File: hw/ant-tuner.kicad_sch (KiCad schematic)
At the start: 4 parts, among them K7702 G2RL-2, K7703 G2RL-2, K7704 G2RL-2

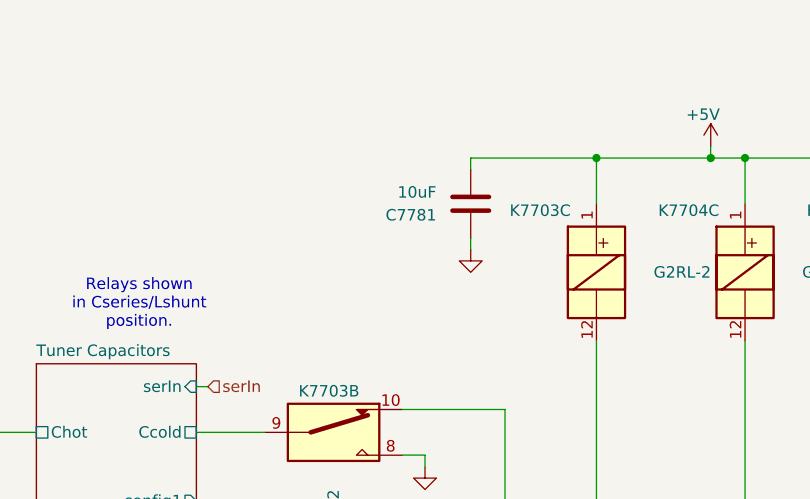
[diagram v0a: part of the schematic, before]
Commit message: Last rites for 800 ohm rx preselector, and probably the RF deck which was stillborn
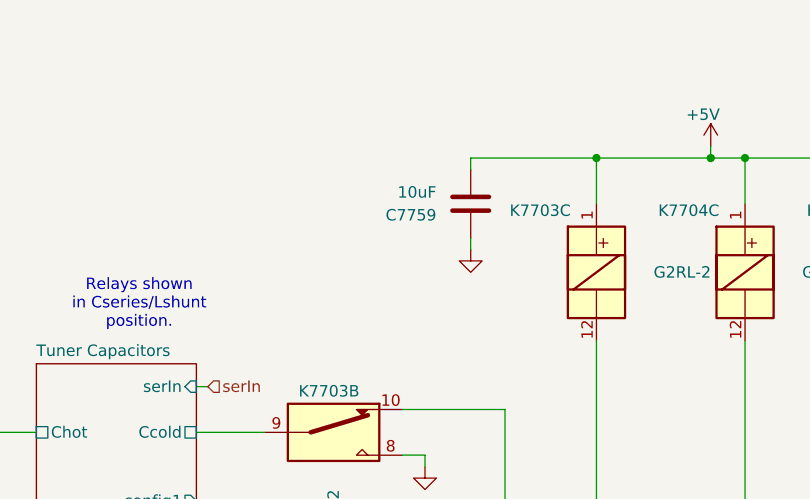
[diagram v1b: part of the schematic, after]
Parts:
- renumbered C7781 to C7759
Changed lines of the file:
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@@
 	(title_block
 		(title "Antenna Tuner")
-		(date "2025-10-30")
+		(date "2025-10-13")
 		(company "WB7NAB")
 		(comment 1 "Alan Mimms")
@@
 		(dnp no)
 		(fields_autoplaced yes)
-		(property "Reference" "#PWR07847"
+		(property "Reference" "#PWR07787"
 			(at 107.95 49.53 0)
 			(effects
@@
 			(project ""
 				(path "/8ae46c04-d01a-4756-8774-512b694bfaff/2406d03c-531b-4eaf-8b4b-4b266b9d0f2b/99bbdde6-e23e-4e3f-9a6c-8b2d863ddc64"
-					(reference "#PWR07847")
+					(reference "#PWR07787")
 					(unit 1)
 				)
@@
 		(dnp no)
 		(fields_autoplaced yes)
-		(property "Reference" "#PWR07846"
+		(property "Reference" "#PWR07786"
 			(at 105.41 106.68 0)
 			(effects
@@
 			(project "NexRig"
 				(path "/8ae46c04-d01a-4756-8774-512b694bfaff/2406d03c-531b-4eaf-8b4b-4b266b9d0f2b/99bbdde6-e23e-4e3f-9a6c-8b2d863ddc64"
-					(reference "#PWR07846")
+					(reference "#PWR07786")
 					(unit 1)
 				)
@@
 		(dnp no)
 		(fields_autoplaced yes)
-		(property "Reference" "#PWR07845"
+		(property "Reference" "#PWR07785"
 			(at 102.87 73.66 0)
 			(effects
@@
 			(project "NexRig"
 				(path "/8ae46c04-d01a-4756-8774-512b694bfaff/2406d03c-531b-4eaf-8b4b-4b266b9d0f2b/99bbdde6-e23e-4e3f-9a6c-8b2d863ddc64"
-					(reference "#PWR07845")
+					(reference "#PWR07785")
 					(unit 1)
 				)
@@
 		(on_board yes)
 		(dnp no)
-		(property "Reference" "C7781"
+		(property "Reference" "C7759"
 			(at 104.14 39.3701 0)
 			(effects
@@
 			(project "NexRig"
 				(path "/8ae46c04-d01a-4756-8774-512b694bfaff/2406d03c-531b-4eaf-8b4b-4b266b9d0f2b/99bbdde6-e23e-4e3f-9a6c-8b2d863ddc64"
-					(reference "C7781")
+					(reference "C7759")
 					(unit 1)
 				)
@@
 		(on_board yes)
 		(dnp no)
-		(property "Reference" "#PWR07848"
+		(property "Reference" "#PWR07788"
 			(at 134.62 35.56 0)
 			(effects
@@
 			(project "NexRig"
 				(path "/8ae46c04-d01a-4756-8774-512b694bfaff/2406d03c-531b-4eaf-8b4b-4b266b9d0f2b/99bbdde6-e23e-4e3f-9a6c-8b2d863ddc64"
-					(reference "#PWR07848")
+					(reference "#PWR07788")
 					(unit 1)
 				)

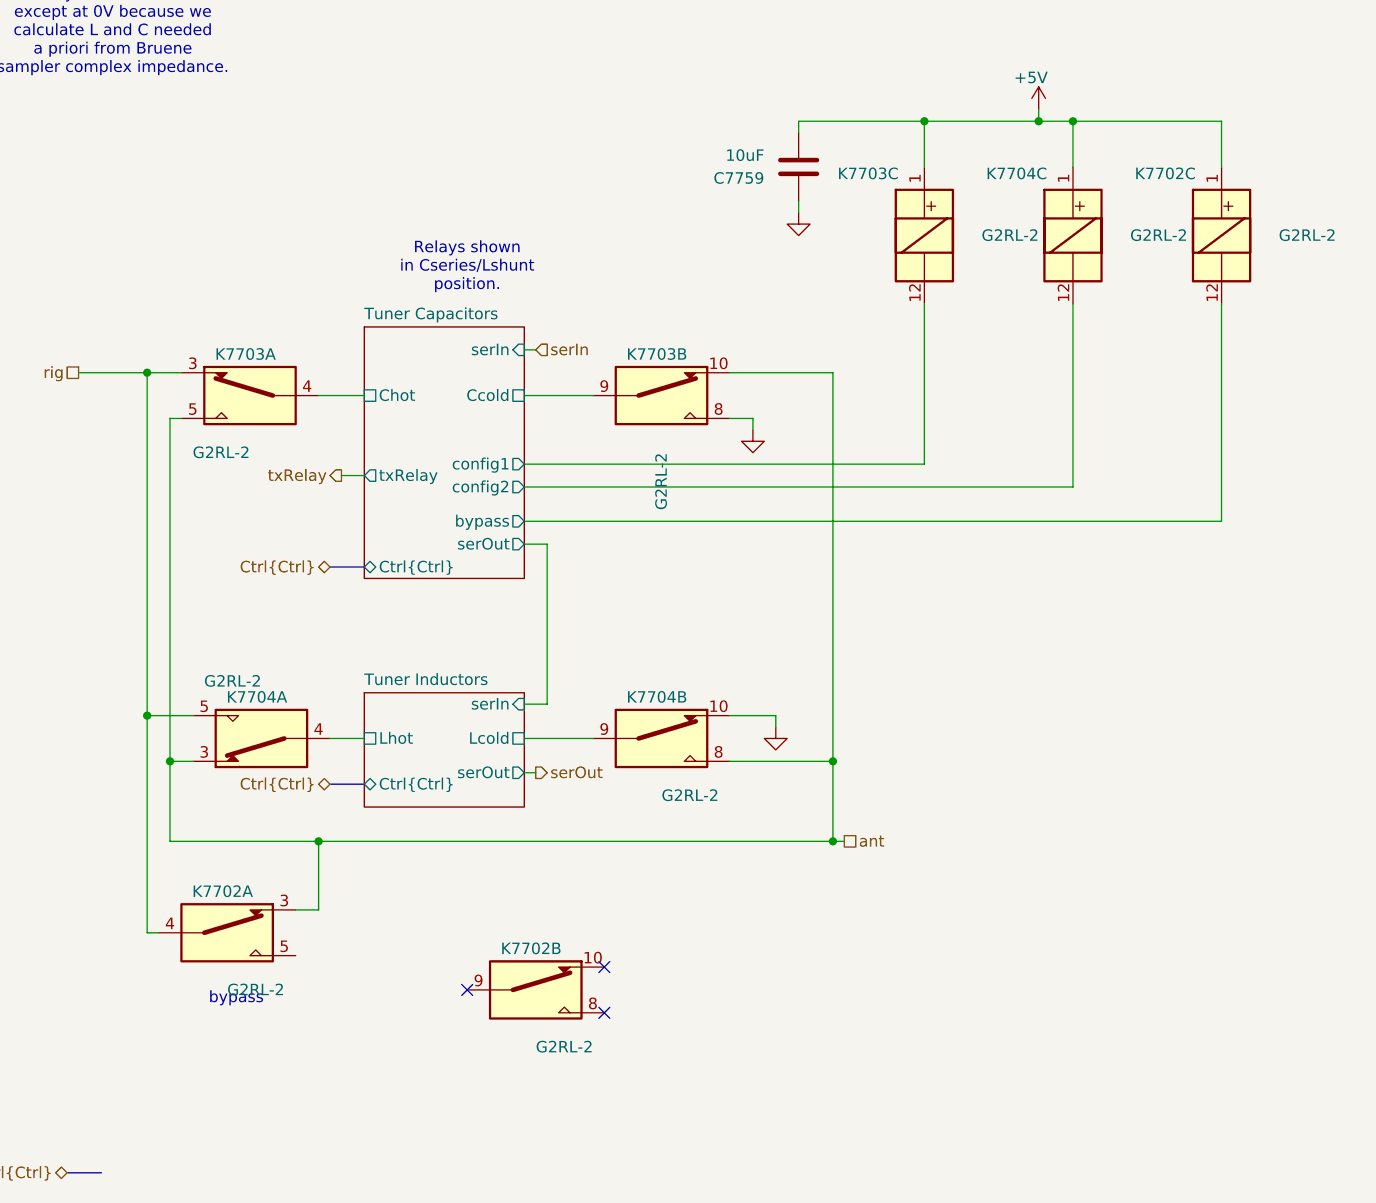
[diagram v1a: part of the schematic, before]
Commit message: Fixed GPIO assignments. Fixed symbol for GRL2-2 relays.
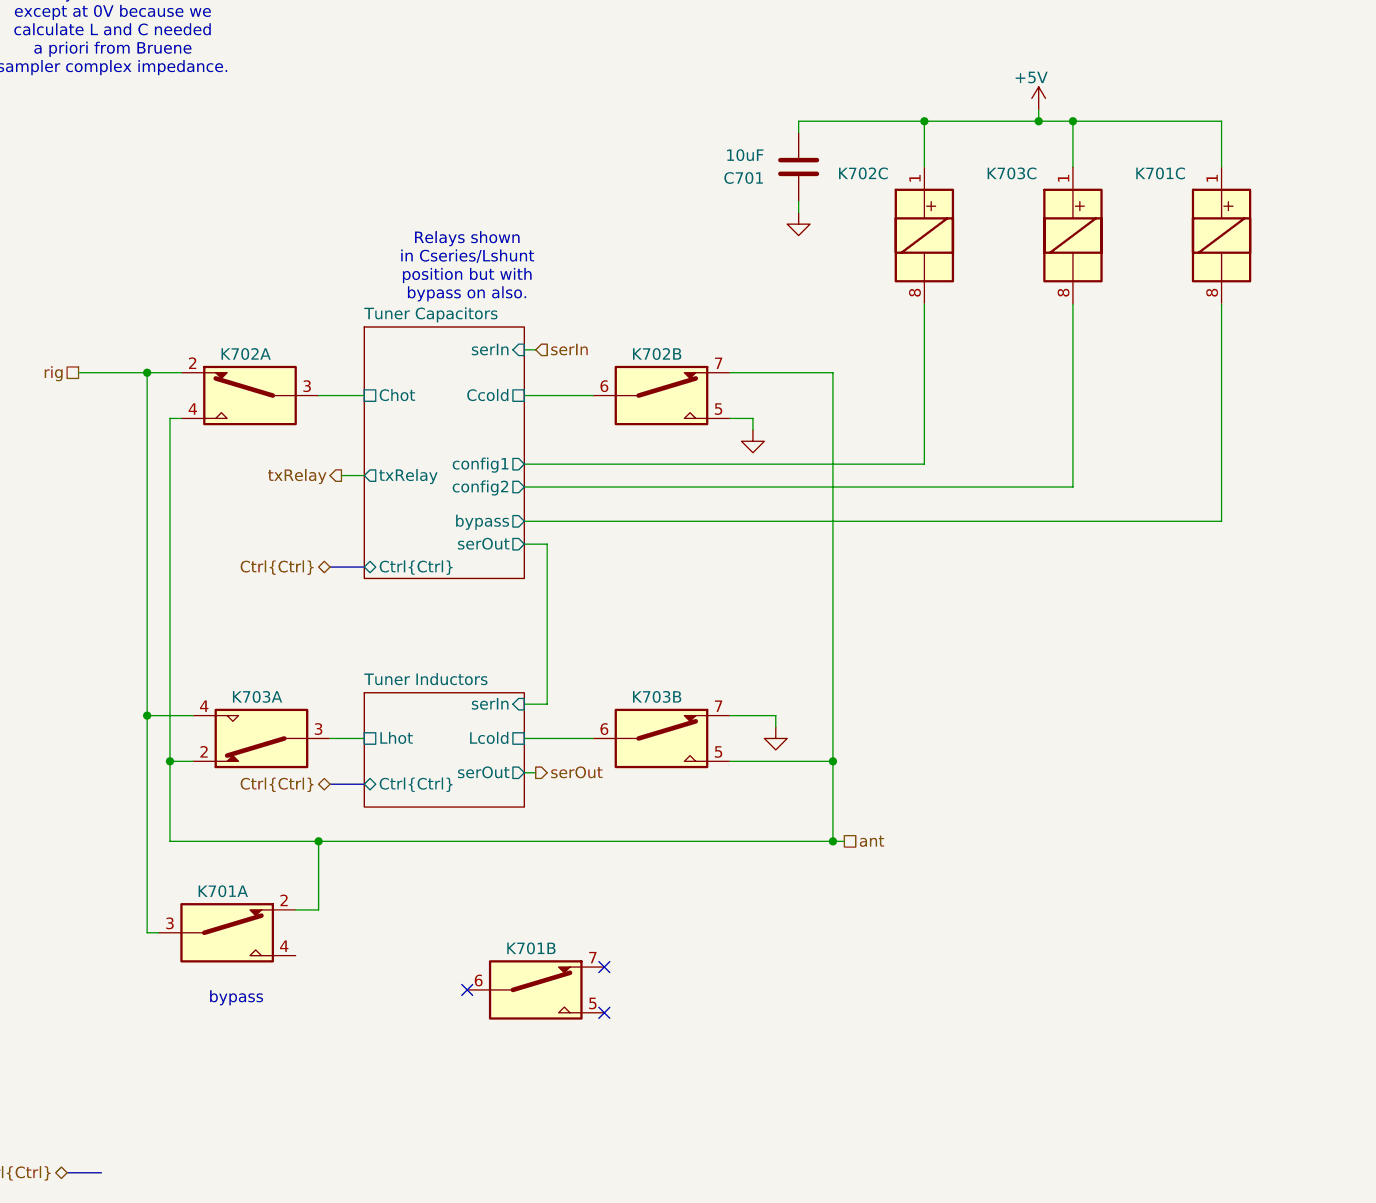
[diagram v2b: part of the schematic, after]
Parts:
- C701: renamed from C7759; working-voltage (none) -> 10V
- K701: renamed from K7702; footprint Relay_THT:Relay_DPDT_Omron_G2RL-2 -> Library:Relay_DPDT_Omron_G2RL-2
- K702: renamed from K7703; footprint Relay_THT:Relay_DPDT_Omron_G2RL-2 -> Library:Relay_DPDT_Omron_G2RL-2
- K703: renamed from K7704; footprint Relay_THT:Relay_DPDT_Omron_G2RL-2 -> Library:Relay_DPDT_Omron_G2RL-2
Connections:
- net GND: now also K702.5, K703.7; no longer K702.8, K703.10
- net Tuner Capacitors/Ccold: now also K702.6; no longer K702.9
- net Tuner Capacitors/Chot: now also K702.3; no longer K702.4
- net Tuner Capacitors/bypass: now also K701.8; no longer K701.12
- net Tuner Capacitors/config1: now also K702.8; no longer K702.12
- net Tuner Capacitors/config2: now also K703.8; no longer K703.12
- net Tuner Inductors/Lcold: now also K703.6; no longer K703.9
- net Tuner Inductors/Lhot: now also K703.3; no longer K703.4
- net ant: now also K701.2, K702.4, K702.7, K703.2, K703.5; no longer K701.3, K702.10, K702.5, K703.3, K703.8
- net rig: now also K701.3, K702.2, K703.4; no longer K701.4, K702.3, K703.5
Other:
- note added: "Relays shown in Cseries/Lshunt position but with bypass on also."
- note removed: "Relays shown in Cseries/Lshunt position."
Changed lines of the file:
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@@
 		)
 	)
-	(text "Relays shown\nin Cseries/Lshunt\nposition."
+	(text "Relays shown\nin Cseries/Lshunt\nposition but with\nbypass on also."
 		(exclude_from_sim no)
 		(at 71.12 49.276 0)
@@
 		(on_board yes)
 		(dnp no)
-		(property "Reference" "K7702"
+		(property "Reference" "K701"
 			(at 78.232 124.968 90)
 			(effects
@@
 				)
 				(justify left)
-			)
-		)
-		(property "Footprint" "Relay_THT:Relay_DPDT_Omron_G2RL-2"
+				(hide yes)
+			)
+		)
+		(property "Footprint" "Library:Relay_DPDT_Omron_G2RL-2"
 			(at 58.674 113.284 0)
 			(effects
@@
 		(pin "4"
 		)
-		(pin "12"
-		)
-		(pin "10"
-		)
-		(pin "9"
+		(pin "7"
+		)
+		(pin "6"
+		)
+		(pin "2"
 		)
 		(pin "8"
@@
 			(project "NexRig"
 				(path "/8ae46c04-d01a-4756-8774-512b694bfaff/2406d03c-531b-4eaf-8b4b-4b266b9d0f2b/99bbdde6-e23e-4e3f-9a6c-8b2d863ddc64"
-					(reference "K7702")
+					(reference "K701")
 					(unit 2)
 				)
@@
 		(dnp no)
 		(fields_autoplaced yes)
-		(property "Reference" "#PWR07787"
+		(property "Reference" "#PWR0703"
 			(at 107.95 49.53 0)
 			(effects
@@
 			(project ""
 				(path "/8ae46c04-d01a-4756-8774-512b694bfaff/2406d03c-531b-4eaf-8b4b-4b266b9d0f2b/99bbdde6-e23e-4e3f-9a6c-8b2d863ddc64"
-					(reference "#PWR07787")
+					(reference "#PWR0703")
 					(unit 1)
 				)
@@
 		(on_board yes)
 		(dnp no)
-		(property "Reference" "K7703"
+		(property "Reference" "K702"
 			(at 112.268 38.862 0)
 			(effects
@@
 				)
 				(justify left)
-			)
-		)
-		(property "Footprint" "Relay_THT:Relay_DPDT_Omron_G2RL-2"
+				(hide yes)
+			)
+		)
+		(property "Footprint" "Library:Relay_DPDT_Omron_G2RL-2"
 			(at 105.664 65.786 0)
 			(effects
@@
 			)
 		)
-		(pin "10"
+		(pin "2"
 		)
 		(pin "8"
 		)
-		(pin "12"
-		)
-		(pin "9"
+		(pin "7"
+		)
+		(pin "6"
 		)
 		(pin "1"
@@
 			(project "NexRig"
 				(path "/8ae46c04-d01a-4756-8774-512b694bfaff/2406d03c-531b-4eaf-8b4b-4b266b9d0f2b/99bbdde6-e23e-4e3f-9a6c-8b2d863ddc64"
-					(reference "K7703")
+					(reference "K702")
 					(unit 3)
 				)
@@
 		(dnp no)
 		(fields_autoplaced yes)
-		(property "Reference" "#PWR07786"
+		(property "Reference" "#PWR0702"
 			(at 105.41 106.68 0)
 			(effects
@@
 			(project "NexRig"
 				(path "/8ae46c04-d01a-4756-8774-512b694bfaff/2406d03c-531b-4eaf-8b4b-4b266b9d0f2b/99bbdde6-e23e-4e3f-9a6c-8b2d863ddc64"
-					(reference "#PWR07786")
+					(reference "#PWR0702")
 					(unit 1)
 				)
@@
 		(on_board yes)
 		(dnp no)
-		(property "Reference" "K7704"
+		(property "Reference" "K703"
 			(at 92.202 97.028 90)
 			(effects
@@
 				)
 				(justify left)
-			)
-		)
-		(property "Footprint" "Relay_THT:Relay_DPDT_Omron_G2RL-2"
+				(hide yes)
+			)
+		)
+		(property "Footprint" "Library:Relay_DPDT_Omron_G2RL-2"
 			(at 72.644 85.344 0)
 			(effects
@@
 		(pin "4"
 		)
-		(pin "10"
-		)
-		(pin "9"
-		)
-		(pin "12"
+		(pin "7"
+		)
+		(pin "6"
+		)
+		(pin "2"
 		)
 		(pin "1"
@@
 			(project "NexRig"
 				(path "/8ae46c04-d01a-4756-8774-512b694bfaff/2406d03c-531b-4eaf-8b4b-4b266b9d0f2b/99bbdde6-e23e-4e3f-9a6c-8b2d863ddc64"
-					(reference "K7704")
+					(reference "K703")
 					(unit 2)
 				)
@@
 		(on_board yes)
 		(dnp no)
-		(property "Reference" "K7702"
+		(property "Reference" "K701"
 			(at 145.288 38.862 0)
 			(effects
@@
 				)
 				(justify left)
-			)
-		)
-		(property "Footprint" "Relay_THT:Relay_DPDT_Omron_G2RL-2"
+				(hide yes)
+			)
+		)
+		(property "Footprint" "Library:Relay_DPDT_Omron_G2RL-2"
 			(at 138.684 65.786 0)
 			(effects
@@
 		(pin "4"
 		)
-		(pin "10"
-		)
-		(pin "9"
+		(pin "6"
+		)
+		(pin "7"
 		)
 		(pin "8"
@@
 		(pin "3"
 		)
-		(pin "12"
+		(pin "2"
 		)
 		(pin "5"
@@
 			(project "NexRig"
 				(path "/8ae46c04-d01a-4756-8774-512b694bfaff/2406d03c-531b-4eaf-8b4b-4b266b9d0f2b/99bbdde6-e23e-4e3f-9a6c-8b2d863ddc64"
-					(reference "K7702")
+					(reference "K701")
 					(unit 3)
 				)
@@
 		(on_board yes)
 		(dnp no)
-		(property "Reference" "K7703"
+		(property "Reference" "K702"
 			(at 46.482 58.928 90)
 			(effects
@@
 				)
 				(justify left)
-			)
-		)
-		(property "Footprint" "Relay_THT:Relay_DPDT_Omron_G2RL-2"
+				(hide yes)
+			)
+		)
+		(property "Footprint" "Library:Relay_DPDT_Omron_G2RL-2"
 			(at 67.056 47.244 0)
 			(effects
@@
 		(pin "4"
 		)
-		(pin "10"
+		(pin "6"
 		)
 		(pin "8"
 		)
-		(pin "12"
-		)
-		(pin "9"
+		(pin "7"
+		)
+		(pin "2"
 		)
 		(pin "1"
@@
 			(project "NexRig"
 				(path "/8ae46c04-d01a-4756-8774-512b694bfaff/2406d03c-531b-4eaf-8b4b-4b266b9d0f2b/99bbdde6-e23e-4e3f-9a6c-8b2d863ddc64"
-					(reference "K7703")
+					(reference "K702")
 					(unit 1)
 				)
@@
 		(on_board yes)
 		(dnp no)
-		(property "Reference" "K7704"
+		(property "Reference" "K703"
 			(at 47.752 97.028 90)
 			(effects
@@
 				)
 				(justify left)
-			)
-		)
-		(property "Footprint" "Relay_THT:Relay_DPDT_Omron_G2RL-2"
+				(hide yes)
+			)
+		)
+		(property "Footprint" "Library:Relay_DPDT_Omron_G2RL-2"
 			(at 68.326 117.856 0)
 			(effects
@@
 			)
 		)
-		(pin "12"
-		)
-		(pin "10"
-		)
-		(pin "9"
+		(pin "2"
+		)
+		(pin "7"
+		)
+		(pin "6"
 		)
 		(pin "1"
@@
 			(project "NexRig"
 				(path "/8ae46c04-d01a-4756-8774-512b694bfaff/2406d03c-531b-4eaf-8b4b-4b266b9d0f2b/99bbdde6-e23e-4e3f-9a6c-8b2d863ddc64"
-					(reference "K7704")
+					(reference "K703")
 					(unit 1)
 				)
@@
 		(dnp no)
 		(fields_autoplaced yes)
-		(property "Reference" "#PWR07785"
+		(property "Reference" "#PWR0701"
 			(at 102.87 73.66 0)
 			(effects
@@
 			(project "NexRig"
 				(path "/8ae46c04-d01a-4756-8774-512b694bfaff/2406d03c-531b-4eaf-8b4b-4b266b9d0f2b/99bbdde6-e23e-4e3f-9a6c-8b2d863ddc64"
-					(reference "#PWR07785")
+					(reference "#PWR0701")
 					(unit 1)
 				)
@@
 		(on_board yes)
 		(dnp no)
-		(property "Reference" "C7759"
+		(property "Reference" "C701"
 			(at 104.14 39.3701 0)
 			(effects
@@
 		)
 		(property "Mouser-part-number" ""
+			(at 107.95 38.1 0)
+			(effects
+				(font
+					(size 1.27 1.27)
+				)
+				(hide yes)
+			)
+		)
+		(property "working-voltage" "10V"
 			(at 107.95 38.1 0)
 			(effects
@@
 			(project "NexRig"
 				(path "/8ae46c04-d01a-4756-8774-512b694bfaff/2406d03c-531b-4eaf-8b4b-4b266b9d0f2b/99bbdde6-e23e-4e3f-9a6c-8b2d863ddc64"
-					(reference "C7759")
+					(reference "C701")
 					(unit 1)
 				)
@@
 		(on_board yes)
 		(dnp no)
-		(property "Reference" "#PWR07788"
+		(property "Reference" "#PWR0704"
 			(at 134.62 35.56 0)
 			(effects
@@
 			(project "NexRig"
 				(path "/8ae46c04-d01a-4756-8774-512b694bfaff/2406d03c-531b-4eaf-8b4b-4b266b9d0f2b/99bbdde6-e23e-4e3f-9a6c-8b2d863ddc64"
-					(reference "#PWR07788")
+					(reference "#PWR0704")
 					(unit 1)
 				)
@@
 		(on_board yes)
 		(dnp no)
-		(property "Reference" "K7703"
+		(property "Reference" "K702"
 			(at 92.202 58.928 90)
 			(effects
@@
 				)
 				(justify left)
-			)
-		)
-		(property "Footprint" "Relay_THT:Relay_DPDT_Omron_G2RL-2"
+				(hide yes)
+			)
+		)
+		(property "Footprint" "Library:Relay_DPDT_Omron_G2RL-2"
 			(at 72.644 47.244 0)
 			(effects
@@
 			)
 		)
-		(pin "10"
-		)
-		(pin "9"
+		(pin "2"
+		)
+		(pin "7"
 		)
 		(pin "1"
 		)
-		(pin "12"
+		(pin "6"
 		)
 		(pin "4"
@@
 			(project "NexRig"
 				(path "/8ae46c04-d01a-4756-8774-512b694bfaff/2406d03c-531b-4eaf-8b4b-4b266b9d0f2b/99bbdde6-e23e-4e3f-9a6c-8b2d863ddc64"
-					(reference "K7703")
+					(reference "K702")
 					(unit 2)
 				)
@@
 		(on_board yes)
 		(dnp no)
-		(property "Reference" "K7702"
+		(property "Reference" "K701"
 			(at 43.942 118.618 90)
 			(effects
@@
 				)
 				(justify left)
-			)
-		)
-		(property "Footprint" "Relay_THT:Relay_DPDT_Omron_G2RL-2"
+				(hide yes)
+			)
+		)
+		(property "Footprint" "Library:Relay_DPDT_Omron_G2RL-2"
 			(at 24.384 106.934 0)
 			(effects
@@
 		(pin "4"
 		)
-		(pin "12"
-		)
-		(pin "10"
-		)
-		(pin "9"
+		(pin "6"
+		)
+		(pin "7"
+		)
+		(pin "2"
 		)
 		(pin "8"
@@
 			(project "NexRig"
 				(path "/8ae46c04-d01a-4756-8774-512b694bfaff/2406d03c-531b-4eaf-8b4b-4b266b9d0f2b/99bbdde6-e23e-4e3f-9a6c-8b2d863ddc64"
-					(reference "K7702")
+					(reference "K701")
 					(unit 1)
 				)
@@
 		(on_board yes)
 		(dnp no)
-		(property "Reference" "K7704"
+		(property "Reference" "K703"
 			(at 128.778 38.862 0)
 			(effects
@@
 				)
 				(justify left)
-			)
-		)
-		(property "Footprint" "Relay_THT:Relay_DPDT_Omron_G2RL-2"
+				(hide yes)
+			)
+		)
+		(property "Footprint" "Library:Relay_DPDT_Omron_G2RL-2"
 			(at 122.174 65.786 0)
 			(effects
@@
 		(pin "4"
 		)
-		(pin "10"
+		(pin "2"
 		)
 		(pin "1"
 		)
-		(pin "12"
-		)
-		(pin "9"
+		(pin "6"
+		)
+		(pin "7"
 		)
 		(pin "8"
@@
 			(project "NexRig"
 				(path "/8ae46c04-d01a-4756-8774-512b694bfaff/2406d03c-531b-4eaf-8b4b-4b266b9d0f2b/99bbdde6-e23e-4e3f-9a6c-8b2d863ddc64"
-					(reference "K7704")
+					(reference "K703")
 					(unit 3)
 				)
